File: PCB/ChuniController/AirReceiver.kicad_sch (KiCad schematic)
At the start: 2 parts

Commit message: PCB + CAD
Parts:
- R1: renamed from R3; footprint (none) -> Resistor_SMD:R_0805_2012Metric_Pad1.20x1.40mm_HandSolder
- R2: renamed from R10; footprint (none) -> Resistor_SMD:R_0805_2012Metric_Pad1.20x1.40mm_HandSolder
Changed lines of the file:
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@@
 		(dnp no)
 		(fields_autoplaced yes)
-		(property "Reference" "R10"
+		(property "Reference" "R2"
 			(at 40.64 45.72 90)
 			(show_name no)
@@
 			)
 		)
-		(property "Footprint" ""
+		(property "Footprint" "Resistor_SMD:R_0805_2012Metric_Pad1.20x1.40mm_HandSolder"
 			(at 40.64 53.848 90)
 			(hide yes)
@@
 			(project "ChuniController"
 				(path "/78a07370-9529-4114-be30-8ab9d3e7e0cd/4dd27aa0-f8f0-4f19-b021-a4827a7a836a"
-					(reference "R10")
+					(reference "R2")
 					(unit 1)
 				)
@@
 		(dnp no)
 		(fields_autoplaced yes)
-		(property "Reference" "R3"
+		(property "Reference" "R1"
 			(at 33.02 45.72 90)
 			(show_name no)
@@
 			)
 		)
-		(property "Footprint" ""
+		(property "Footprint" "Resistor_SMD:R_0805_2012Metric_Pad1.20x1.40mm_HandSolder"
 			(at 33.02 53.848 90)
 			(hide yes)
@@
 			(project "ChuniController"
 				(path "/78a07370-9529-4114-be30-8ab9d3e7e0cd/4dd27aa0-f8f0-4f19-b021-a4827a7a836a"
-					(reference "R3")
+					(reference "R1")
 					(unit 1)
 				)

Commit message: PCB
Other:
- moved on the sheet: R1, R2

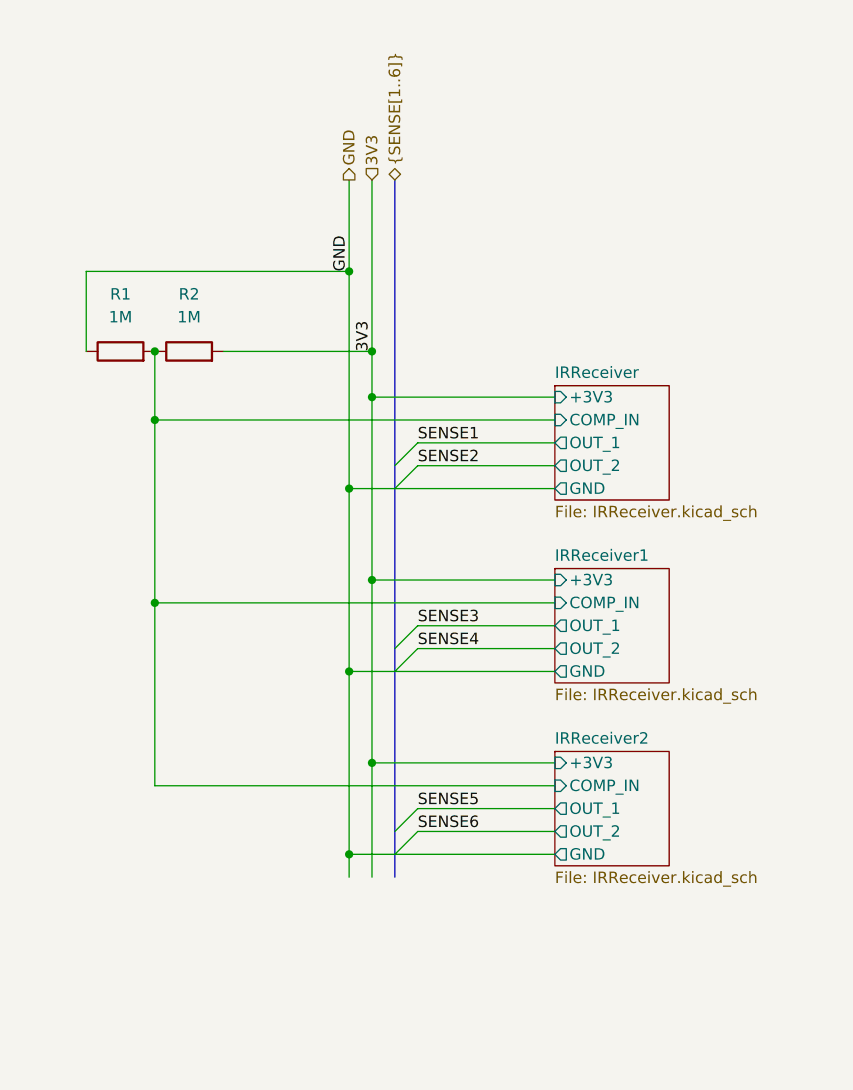
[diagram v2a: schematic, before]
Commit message: PCB both ir board: ok add LM393D 3d model
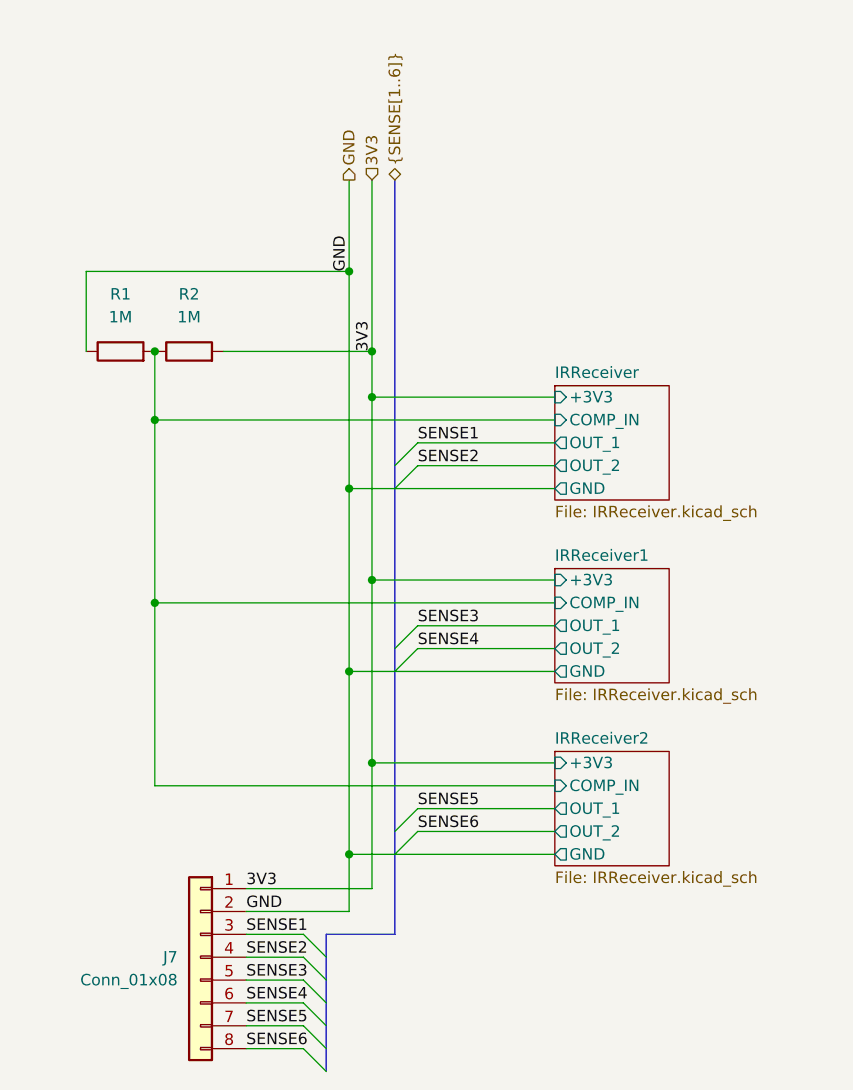
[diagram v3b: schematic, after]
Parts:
- added J7: Conn_01x08, Connector_JST:JST_SH_SM08B-SRSS-TB_1x08-1MP_P1.00mm_Horizontal, symbol Connector_Generic:Conn_01x08
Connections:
- net 3V3: now also J7.1 (Pin_1)
- net GND: now also J7.2 (Pin_2)
- net SENSE1: now also J7.3 (Pin_3)
- net SENSE2: now also J7.4 (Pin_4)
- net SENSE3: now also J7.5 (Pin_5)
- net SENSE4: now also J7.6 (Pin_6)
- net SENSE5: now also J7.7 (Pin_7)
- net SENSE6: now also J7.8 (Pin_8)

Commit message: PCB
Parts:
- removed J7: Conn_01x08, Connector_JST:JST_SH_SM08B-SRSS-TB_1x08-1MP_P1.00mm_Horizontal, symbol Connector_Generic:Conn_01x08
